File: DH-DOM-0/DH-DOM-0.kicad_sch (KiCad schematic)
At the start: 43 parts, among them J1 USB_C_Receptacle_USB2.0_14P, J2 Conn_01x02, Q1 FDN340P, SW1 RST, SW2 BOOT, U1 LSM6DSOXTR, U2 MMC5983MA, U3 BMI270, U4 NCP1117-3.3_SOT223, U5 TVS1400DRV, U6 ESP32-S3-WROOM-1-N4R8, U7 TP4057, U8 ST7789, U9 LSM6DSV16BTR

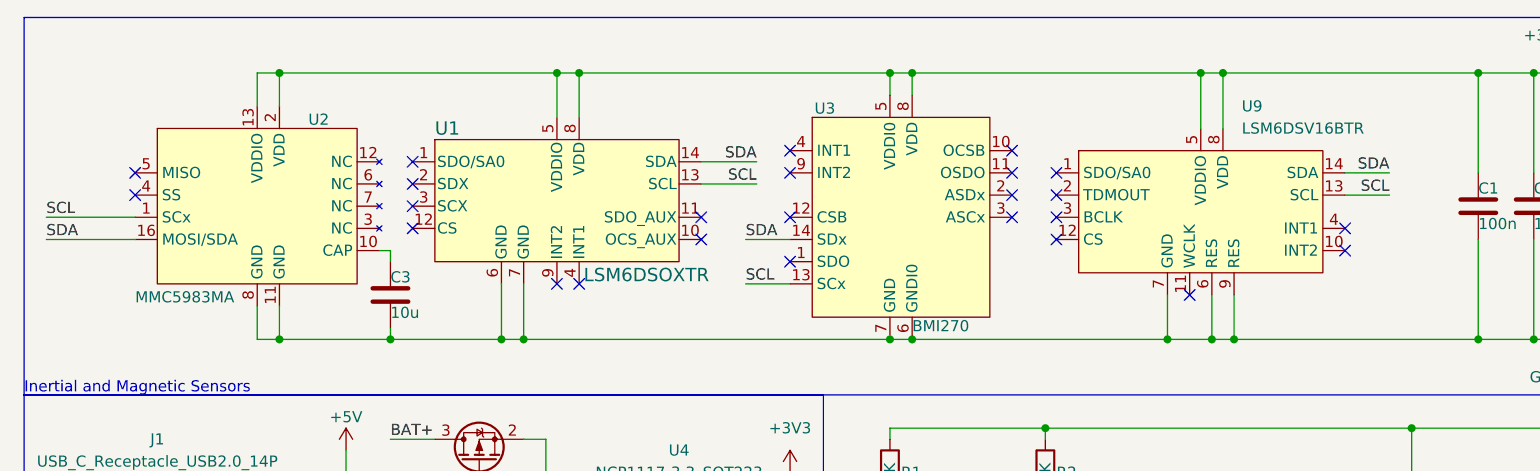
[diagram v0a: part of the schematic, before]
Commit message: edit
separate versions for different IMUs, same footprint but traces have miniscule differences.
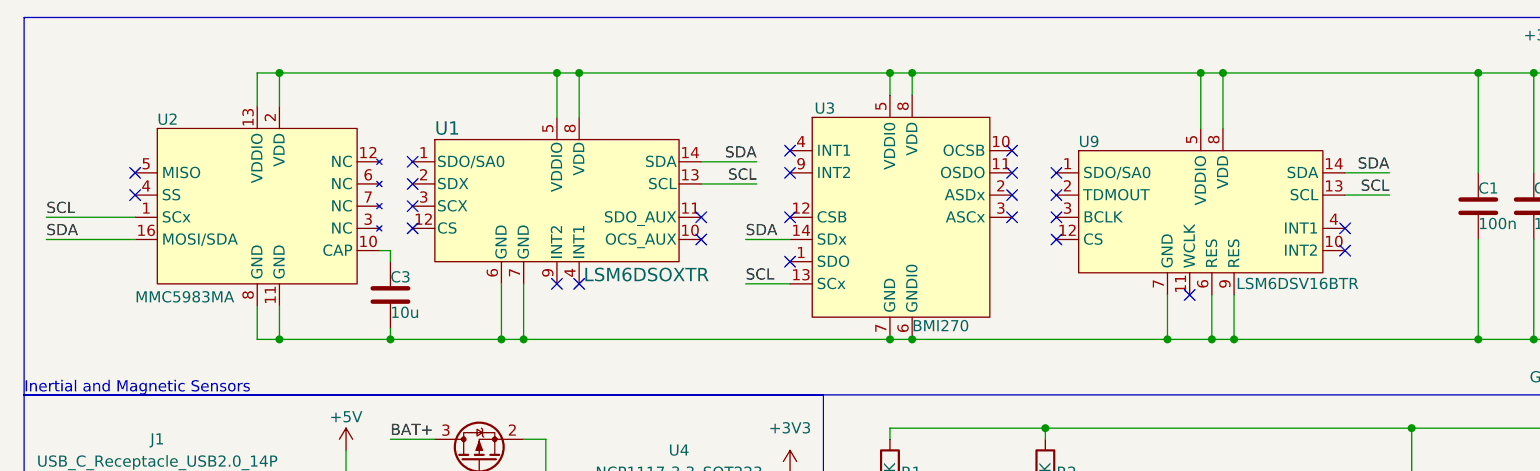
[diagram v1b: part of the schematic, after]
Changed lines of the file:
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@@
 	)
 	(junction
-		(at 171.45 59.69)
-		(diameter 0)
-		(color 0 0 0 0)
-	)
-	(junction
 		(at 54.61 133.35)
 		(diameter 0)
@@
 	)
 	(junction
+		(at 116.84 69.85)
+		(diameter 0)
+		(color 0 0 0 0)
+	)
+	(junction
 		(at 49.53 68.58)
 		(diameter 0)
@@
 	)
 	(junction
+		(at 171.45 123.19)
+		(diameter 0)
+		(color 0 0 0 0)
+	)
+	(junction
 		(at 62.23 157.48)
 		(diameter 0)
@@
 	)
 	(junction
+		(at 134.62 74.93)
+		(diameter 0)
+		(color 0 0 0 0)
+	)
+	(junction
 		(at 50.8 157.48)
 		(diameter 0)
@@
 	)
 	(junction
-		(at 116.84 69.85)
+		(at 171.45 59.69)
 		(diameter 0)
 		(color 0 0 0 0)
@@
 	)
 	(junction
-		(at 171.45 123.19)
-		(diameter 0)
-		(color 0 0 0 0)
-	)
-	(junction
 		(at 39.37 157.48)
 		(diameter 0)
@@
 	)
 	(junction
-		(at 134.62 74.93)
-		(diameter 0)
-		(color 0 0 0 0)
-	)
-	(junction
 		(at 43.18 157.48)
 		(diameter 0)
@@
 		(exclude_from_sim no)
 		(in_bom yes)
-		(on_board yes)
+		(on_board no)
 		(in_pos_files yes)
 		(dnp no)
@@
 		(exclude_from_sim no)
 		(in_bom yes)
-		(on_board yes)
+		(on_board no)
 		(in_pos_files yes)
 		(dnp no)
@@
 		(exclude_from_sim no)
 		(in_bom yes)
-		(on_board no)
+		(on_board yes)
 		(in_pos_files yes)
 		(dnp no)
-		(fields_autoplaced yes)
 		(property "Reference" "U9"
-			(at 152.0033 22.86 0)
+			(at 133.35 26.924 0)
 			(show_name no)
 			(do_not_autoplace no)
@@
 		)
 		(property "Value" "LSM6DSV16BTR"
-			(at 152.0033 25.4 0)
+			(at 151.384 43.18 0)
 			(show_name no)
 			(do_not_autoplace no)
@@
 		(dnp no)
 		(property "Reference" "U2"
-			(at 45.212 24.384 0)
+			(at 27.94 24.384 0)
 			(show_name no)
 			(do_not_autoplace no)

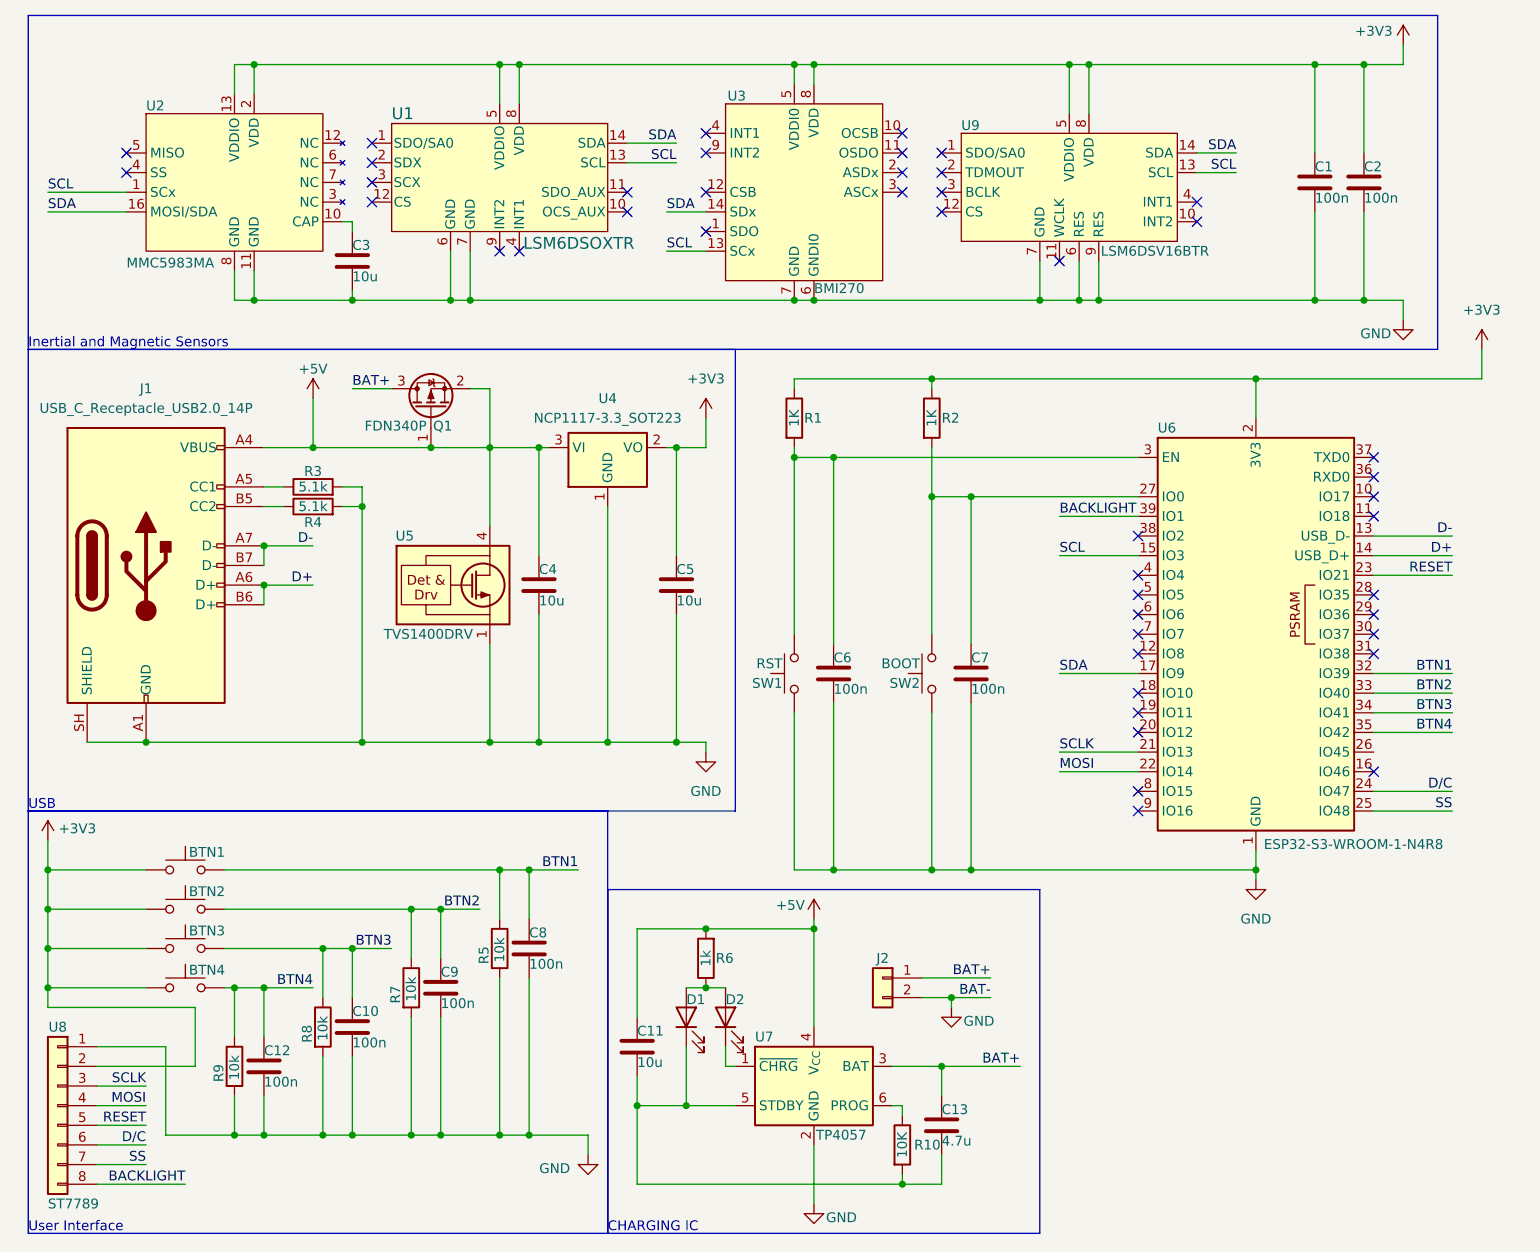
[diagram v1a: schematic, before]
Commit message: edit
put everything on top layer 3v3 cap
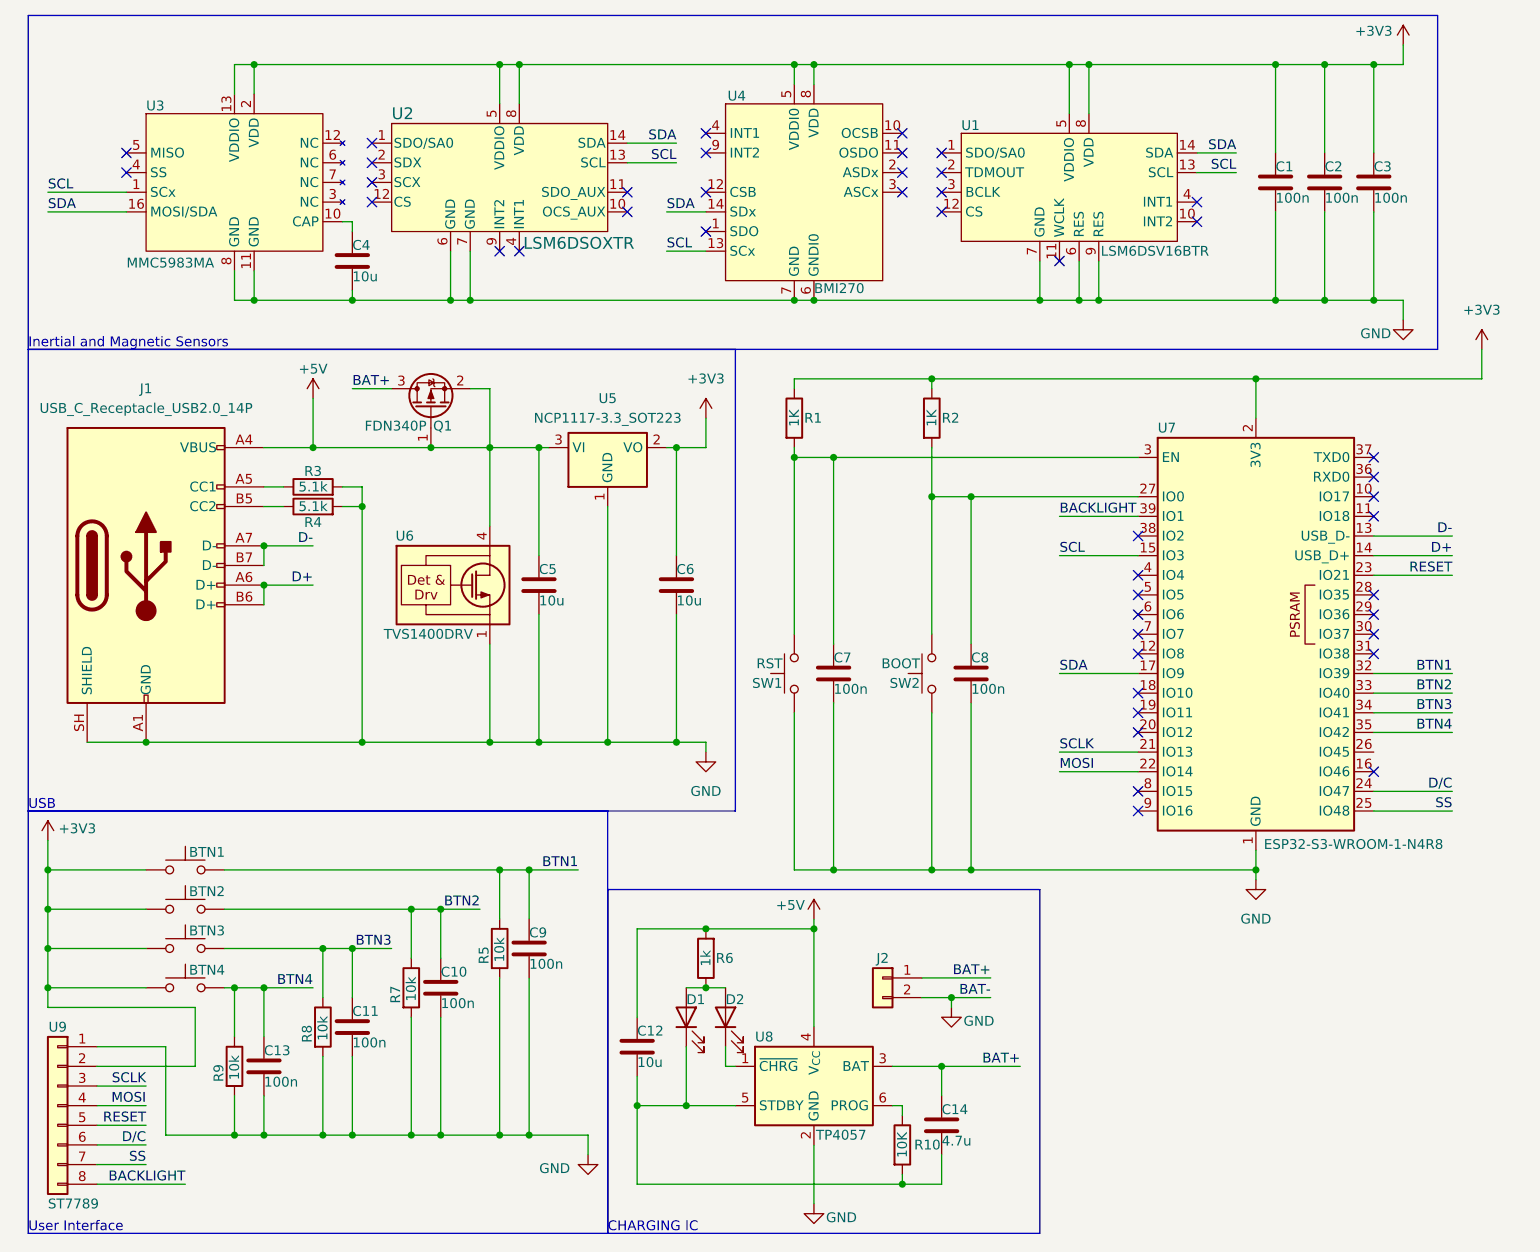
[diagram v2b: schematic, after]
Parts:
- added C3: 100n, Capacitor_SMD:C_0805_2012Metric, symbol Device:C
- renumbered C9 to C10, C10 to C11, C11 to C12, C12 to C13, C13 to C14, C3 to C4, C4 to C5, C5 to C6, C6 to C7, C7 to C8, C8 to C9, U9 to U1, U1 to U2, U2 to U3, U3 to U4, U4 to U5, U5 to U6, U6 to U7, U7 to U8, U8 to U9
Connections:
- net +3V3: now also C3.1
- net GND: now also C3.2
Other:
- moved on the sheet: C1, C2

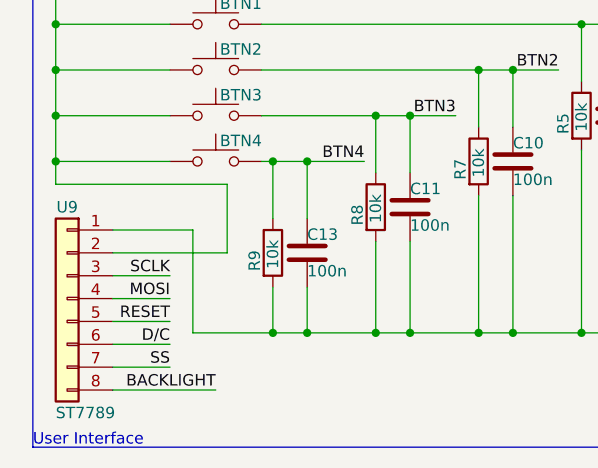
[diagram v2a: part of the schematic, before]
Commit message: edit
new header pitch
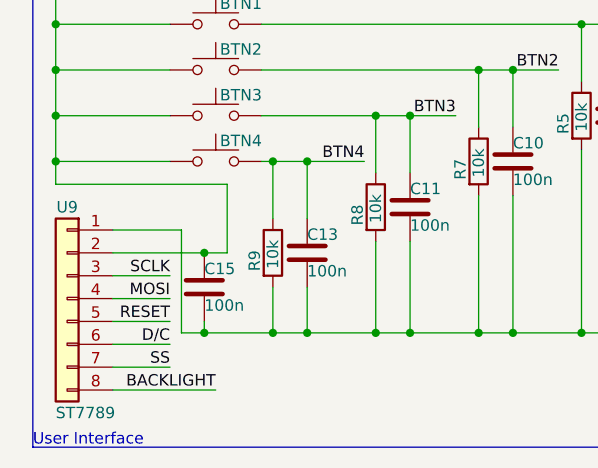
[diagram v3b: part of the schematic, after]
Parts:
- added C15: 100n, Capacitor_SMD:C_0805_2012Metric, symbol Device:C
- BTN1, BTN2, BTN3, BTN4, J2: footprint Connector_PinHeader_2.54mm:PinHeader_2x01_P2.54mm_Vertical -> Connector_PinHeader_2.00mm:PinHeader_2x01_P2.00mm_Vertical
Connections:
- net +3V3: now also C15.1
- net GND: now also C15.2
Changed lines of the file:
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@@
 	)
 	(junction
+		(at 31.75 148.59)
+		(diameter 0)
+		(color 0 0 0 0)
+	)
+	(junction
 		(at 114.3 19.05)
 		(diameter 0)
@@
 	)
 	(junction
-		(at 39.37 157.48)
+		(at 73.66 19.05)
 		(diameter 0)
 		(color 0 0 0 0)
 	)
 	(junction
-		(at 73.66 19.05)
+		(at 143.51 49.53)
 		(diameter 0)
 		(color 0 0 0 0)
 	)
 	(junction
-		(at 143.51 49.53)
+		(at 78.74 106.68)
 		(diameter 0)
 		(color 0 0 0 0)
 	)
 	(junction
-		(at 78.74 106.68)
+		(at 39.37 157.48)
 		(diameter 0)
 		(color 0 0 0 0)
@@
 		(color 0 0 0 0)
 	)
+	(junction
+		(at 31.75 157.48)
+		(diameter 0)
+		(color 0 0 0 0)
+	)
 	(no_connect
 		(at 76.2 43.18)
@@
 	(wire
 		(pts
+			(xy 31.75 148.59) (xy 34.29 148.59)
+		)
+		(stroke
+			(width 0)
+			(type default)
+		)
+	)
+	(wire
+		(pts
 			(xy 43.18 73.66) (xy 45.72 73.66)
 		)
@@
 	(wire
 		(pts
-			(xy 30.48 146.05) (xy 30.48 157.48)
-		)
-		(stroke
-			(width 0)
-			(type default)
-		)
-	)
-	(wire
-		(pts
 			(xy 73.66 123.19) (xy 77.47 123.19)
 		)
@@
 	(wire
 		(pts
+			(xy 31.75 156.21) (xy 31.75 157.48)
+		)
+		(stroke
+			(width 0)
+			(type default)
+		)
+	)
+	(wire
+		(pts
 			(xy 53.34 73.66) (xy 55.88 73.66)
 		)
@@
 	(wire
 		(pts
-			(xy 21.59 146.05) (xy 30.48 146.05)
+			(xy 21.59 146.05) (xy 29.21 146.05)
 		)
 		(stroke
@@
 	(wire
 		(pts
+			(xy 29.21 157.48) (xy 31.75 157.48)
+		)
+		(stroke
+			(width 0)
+			(type default)
+		)
+	)
+	(wire
+		(pts
 			(xy 41.91 49.53) (xy 54.61 49.53)
 		)
@@
 	(wire
 		(pts
+			(xy 31.75 157.48) (xy 39.37 157.48)
+		)
+		(stroke
+			(width 0)
+			(type default)
+		)
+	)
+	(wire
+		(pts
 			(xy 186.69 105.41) (xy 196.85 105.41)
 		)
@@
 	(wire
 		(pts
-			(xy 30.48 157.48) (xy 39.37 157.48)
-		)
-		(stroke
-			(width 0)
-			(type default)
-		)
-	)
-	(wire
-		(pts
 			(xy 171.45 123.19) (xy 171.45 124.46)
 		)
@@
 	(wire
 		(pts
-			(xy 21.59 148.59) (xy 34.29 148.59)
+			(xy 21.59 148.59) (xy 31.75 148.59)
 		)
 		(stroke
@@
 	(wire
 		(pts
+			(xy 29.21 146.05) (xy 29.21 157.48)
+		)
+		(stroke
+			(width 0)
+			(type default)
+		)
+	)
+	(wire
+		(pts
 			(xy 34.29 140.97) (xy 34.29 148.59)
 		)
@@
 	)
 	(symbol
+		(lib_id "Device:C")
+		(at 31.75 152.4 0)
+		(unit 1)
+		(body_style 1)
+		(exclude_from_sim no)
+		(in_bom yes)
+		(on_board yes)
+		(in_pos_files yes)
+		(dnp no)
+		(property "Reference" "C15"
+			(at 31.75 150.368 0)
+			(show_name no)
+			(do_not_autoplace no)
+			(effects
+				(font
+					(size 1.27 1.27)
+				)
+				(justify left)
+			)
+		)
+		(property "Value" "100n"
+			(at 31.75 154.432 0)
+			(show_name no)
+			(do_not_autoplace no)
+			(effects
+				(font
+					(size 1.27 1.27)
+				)
+				(justify left)
+			)
+		)
+		(property "Footprint" "Capacitor_SMD:C_0805_2012Metric"
+			(at 32.7152 156.21 0)
+			(hide yes)
+			(show_name no)
+			(do_not_autoplace no)
+			(effects
+				(font
+					(size 1.27 1.27)
+				)
+			)
+		)
+		(property "Datasheet" ""
+			(at 31.75 152.4 0)
+			(hide yes)
+			(show_name no)
+			(do_not_autoplace no)
+			(effects
+				(font
+					(size 1.27 1.27)
+				)
+			)
+		)
+		(property "Description" "Unpolarized capacitor"
+			(at 31.75 152.4 0)
+			(hide yes)
+			(show_name no)
+			(do_not_autoplace no)
+			(effects
+				(font
+					(size 1.27 1.27)
+				)
+			)
+		)
+		(pin "2"
+		)
+		(pin "1"
+		)
+		(instances
+			(project "DH-DOM-0"
+				(path "/1a16546f-17ba-458f-9ffb-023bbcd494b0"
+					(reference "C15")
+					(unit 1)
+				)
+			)
+		)
+	)
+	(symbol
 		(lib_id "power:+3V3")
 		(at 200.66 55.88 0)
@@
 			)
 		)
-		(property "Footprint" "Connector_PinHeader_2.54mm:PinHeader_2x01_P2.54mm_Vertical"
+		(property "Footprint" "Connector_PinHeader_2.00mm:PinHeader_2x01_P2.00mm_Vertical"
 			(at 33.02 123.19 0)
 			(hide yes)
@@
 			)
 		)
-		(property "Footprint" "Connector_PinHeader_2.54mm:PinHeader_2x01_P2.54mm_Vertical"
+		(property "Footprint" "Connector_PinHeader_2.00mm:PinHeader_2x01_P2.00mm_Vertical"
 			(at 33.02 133.35 0)
 			(hide yes)
@@
 			)
 		)
-		(property "Footprint" "Connector_PinHeader_2.54mm:PinHeader_2x01_P2.54mm_Vertical"
+		(property "Footprint" "Connector_PinHeader_2.00mm:PinHeader_2x01_P2.00mm_Vertical"
 			(at 33.02 118.11 0)
 			(hide yes)
@@
 			)
 		)
-		(property "Footprint" "Connector_PinHeader_2.54mm:PinHeader_2x01_P2.54mm_Vertical"
+		(property "Footprint" "Connector_PinHeader_2.00mm:PinHeader_2x01_P2.00mm_Vertical"
 			(at 33.02 128.27 0)
 			(hide yes)
@@
 			)
 		)
-		(property "Footprint" "Connector_PinHeader_2.54mm:PinHeader_2x01_P2.54mm_Vertical"
+		(property "Footprint" "Connector_PinHeader_2.00mm:PinHeader_2x01_P2.00mm_Vertical"
 			(at 123.19 137.16 0)
 			(hide yes)

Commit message: edit
forgot lowkey
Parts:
- BTN1: footprint Connector_PinHeader_2.00mm:PinHeader_2x01_P2.00mm_Vertical -> Connector_PinHeader_2.00mm:PinHeader_2x01_P2.00mm_Horizontal
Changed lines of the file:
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@@
 			)
 		)
-		(property "Footprint" "Connector_PinHeader_2.00mm:PinHeader_2x01_P2.00mm_Vertical"
+		(property "Footprint" "Connector_PinHeader_2.00mm:PinHeader_2x01_P2.00mm_Horizontal"
 			(at 33.02 118.11 0)
 			(hide yes)
